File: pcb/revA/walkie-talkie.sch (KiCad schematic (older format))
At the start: 141 parts, among them J1 ANT, J2 ICSP, J3 USB_B_Micro, Q1 BFQ67, Q10 BC846B, Q11 BC846B, Q2 BC846B, Q3 BC846B, Q4 BC846B, Q5 2SC3356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

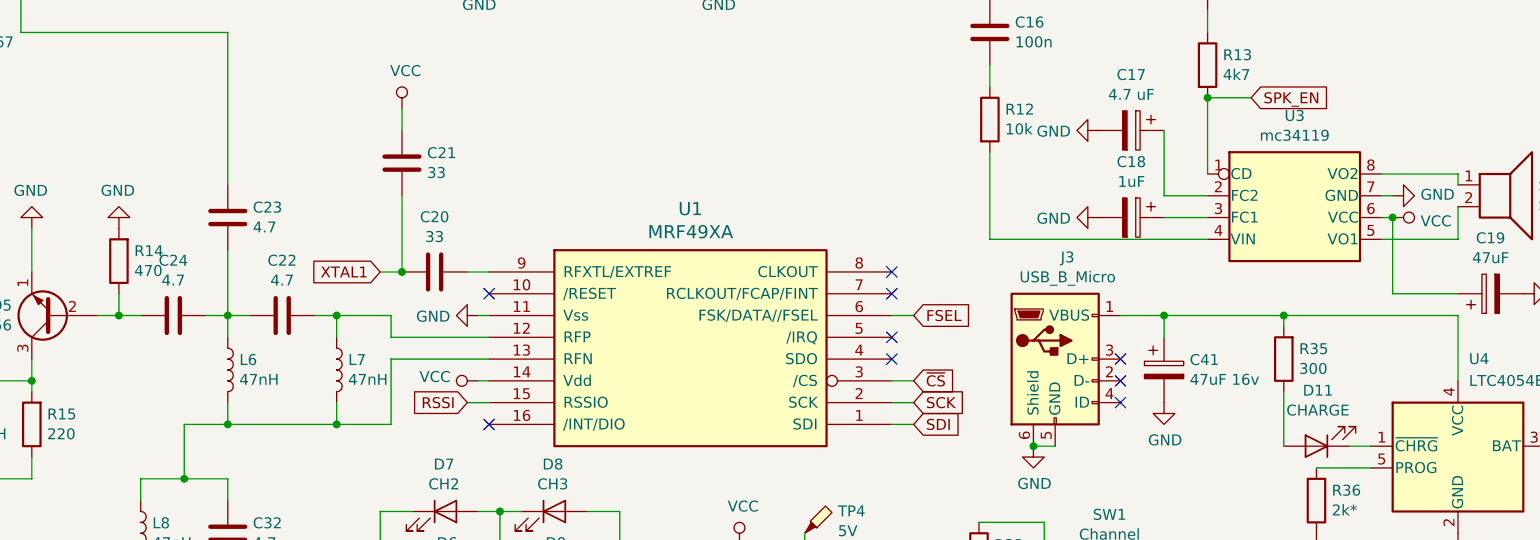
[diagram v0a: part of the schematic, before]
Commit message: Fixed bugs in rev.A
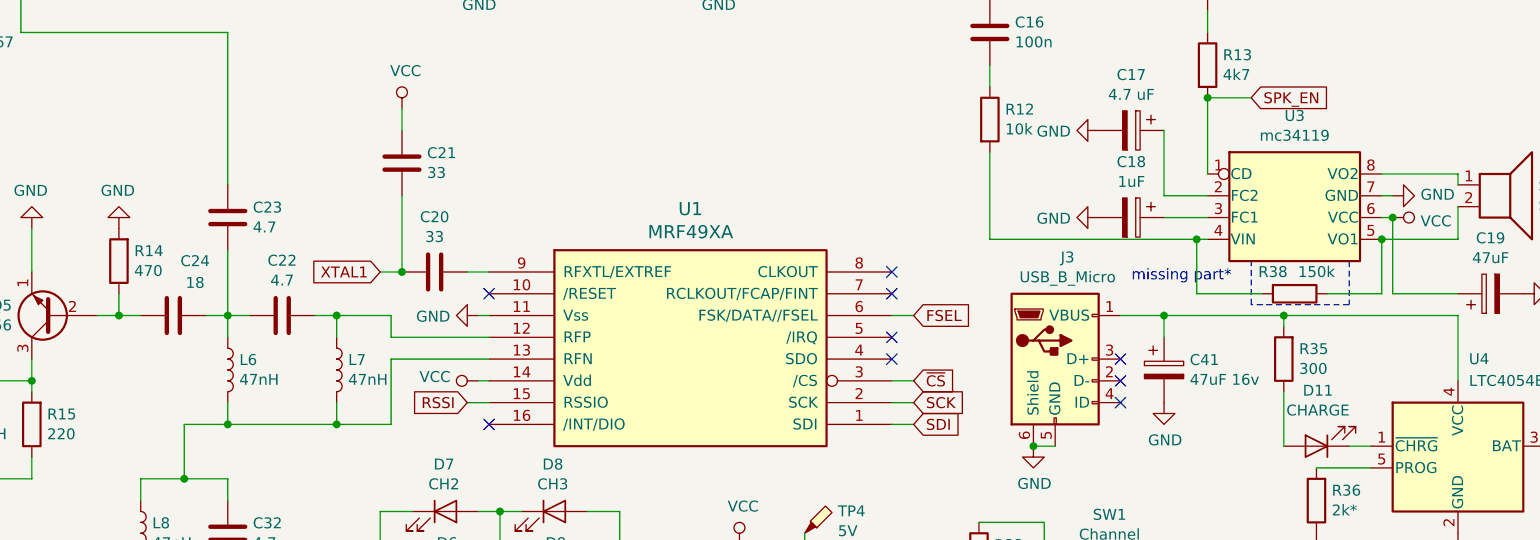
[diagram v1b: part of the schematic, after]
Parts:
- added R38: 150k, Resistor_SMD:R_0805_2012Metric_Pad1.15x1.40mm_HandSolder, symbol Device:R
- C24: value 4.7 -> 18
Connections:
- net at R12.2, U3.4 (VIN): now also R38.2
- net at SP1.2, U3.5 (VO1): now also R38.1
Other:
- note added: "missing part*"
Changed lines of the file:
@@
 U 1 1 5EBE83BC
 P 4250 3350
-F 0 "C24" V 4502 3350 50  0000 C CNN
-F 1 "4.7" V 4411 3350 50  0000 C CNN
+F 0 "C24" V 4500 3250 50  0000 C CNN
+F 1 "18" V 4400 3250 50  0000 C CNN
 F 2 "Capacitor_SMD:C_0805_2012Metric_Pad1.15x1.40mm_HandSolder" H 4288 3200 50  0001 C CNN
 F 3 "~" H 4250 3350 50  0001 C CNN
@@
 	8000 3000 8000 2600
 Wire Wire Line
-	8000 3000 9000 3000
+	8000 3000 8950 3000
 $Comp
 L Device:R R13
@@
 	10400 700  9900 700
 Connection ~ 9900 700
+$Comp
+L Device:R R38
+U 1 1 5EBB265F
+P 9400 3250
+F 0 "R38" V 9300 3150 50  0000 C CNN
+F 1 "150k" V 9300 3350 50  0000 C CNN
+F 2 "Resistor_SMD:R_0805_2012Metric_Pad1.15x1.40mm_HandSolder" V 9330 3250 50  0001 C CNN
+F 3 "~" H 9400 3250 50  0001 C CNN
+	1    9400 3250
+	0    1    1    0
+$EndComp
+Wire Wire Line
+	9250 3250 8950 3250
+Wire Wire Line
+	8950 3250 8950 3000
+Connection ~ 8950 3000
+Wire Wire Line
+	8950 3000 9000 3000
+Wire Wire Line
+	9550 3250 9800 3250
+Wire Wire Line
+	9800 3250 9800 3000
+Connection ~ 9800 3000
+Wire Notes Line
+	9200 3100 9650 3100
+Wire Notes Line
+	9650 3100 9650 3300
+Wire Notes Line
+	9650 3300 9200 3300
+Wire Notes Line
+	9200 3300 9200 3100
+Text Notes 8650 3200 0    50   ~ 0
+missing part*
 $EndSCHEMATC
